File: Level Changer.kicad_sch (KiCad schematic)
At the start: 4 parts, among them Q1 2N7002

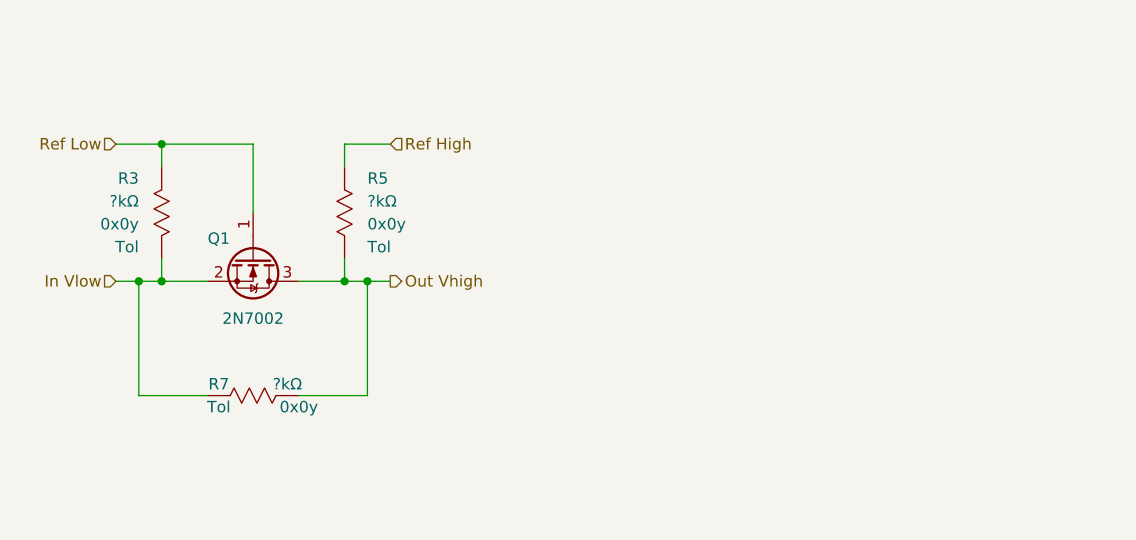
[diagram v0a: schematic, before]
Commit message: Power & Level Translation
Isolated 5VDC changed and a 3.3VDC LDO was added. The original 5VDC was too expensive and big. The new one is still both, but less so.
The level translator is now a dedicated IC instead of MOSFETs. I was having trouble making it work the way I wanted.
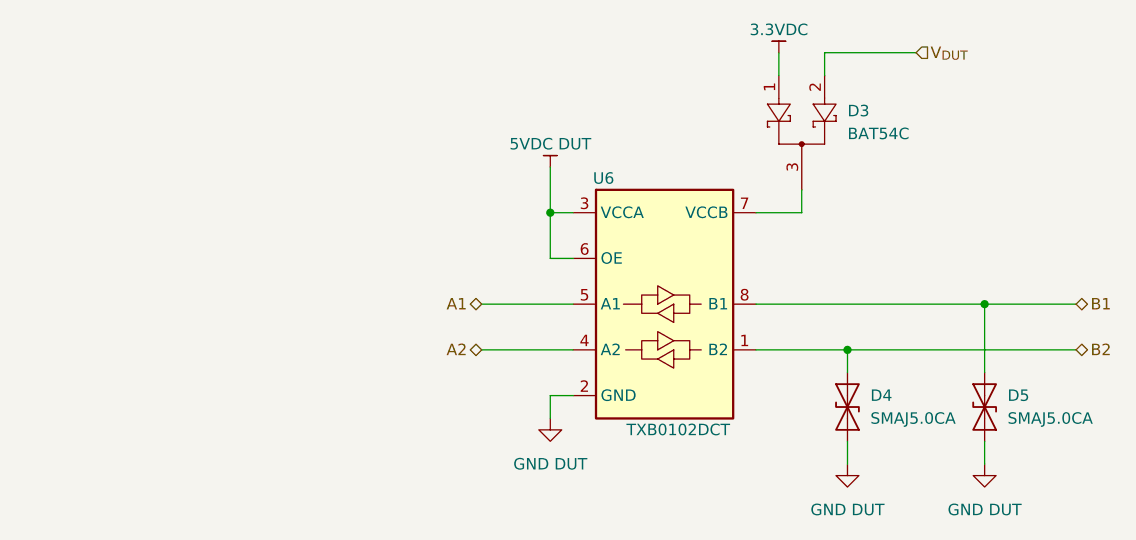
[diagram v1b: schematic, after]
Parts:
- removed Q1: 2N7002, Package_TO_SOT_SMD:SOT-23, symbol Transistor_FET:2N7002
- removed R3, R5, R7: [Resistance] [Footprint] [Tolerance], symbol Prototype Schematic Symbols - Isolated ComPort:Resistor_Template
- added D3: BAT54C, Package_TO_SOT_SMD:SOT-23, symbol Prototype Schematic Symbols - Isolated ComPort:BAT54C
- added D4, D5: SMAJ5.0CA, Diode_SMD:D_SMA, symbol Diode:SMAJ5.0CA
- added U6: TXB0102DCT, Package_SO:TSSOP-8_3x3mm_P0.65mm, symbol Logic_LevelTranslator:TXB0102DCT
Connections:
- new net: D3.3, U6.7 (VCCB)
- new net 3.3VDC: D3.1
- new net 5VDC DUT: U6.3 (VCCA), U6.6 (OE)
- new net A1: U6.5 (A1)
- new net A2: U6.4 (A2)
- new net B1: D5.1 (A1), U6.8 (B1)
- new net B2: D4.1 (A1), U6.1 (B2)
- new net GND DUT: D4.2 (A2), D5.2 (A2), U6.2 (GND)
- new net V_{DUT}: D3.2
